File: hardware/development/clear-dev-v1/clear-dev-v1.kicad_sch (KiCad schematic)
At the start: 86 parts, among them J1 USB_B_Micro, J10 Conn_01x28_Pin, J11 Conn_01x28_Pin, J12 Conn_01x02_Pin, J2 Conn_01x02_Pin, J3 Conn_01x02_Pin, J4 Conn_01x03_Pin, J5 Conn_01x02_Pin, J6 Conn_01x02_Pin, J7 Conn_01x06_Pin, J8 Conn_01x02_Pin, J9 Conn_01x02_Pin, SW1 SW_Push - SKQGADE010, T1 Logo, T2 Logo, U1 FT232H, U10 DS1086LU, U2 SN74LVC1G125DCKR, U3 SN74LVC1G125DCKR, U4 SN74LVC1G125DCKR, U5 TAR5SxxU, U6 TAR5SxxU, U7 W25Q32FVSS, U8 M.2-CONNECTOR-E, U9 TMUX4053-BQB, X1 DSC6001_10MHZ, Y1 12MHz

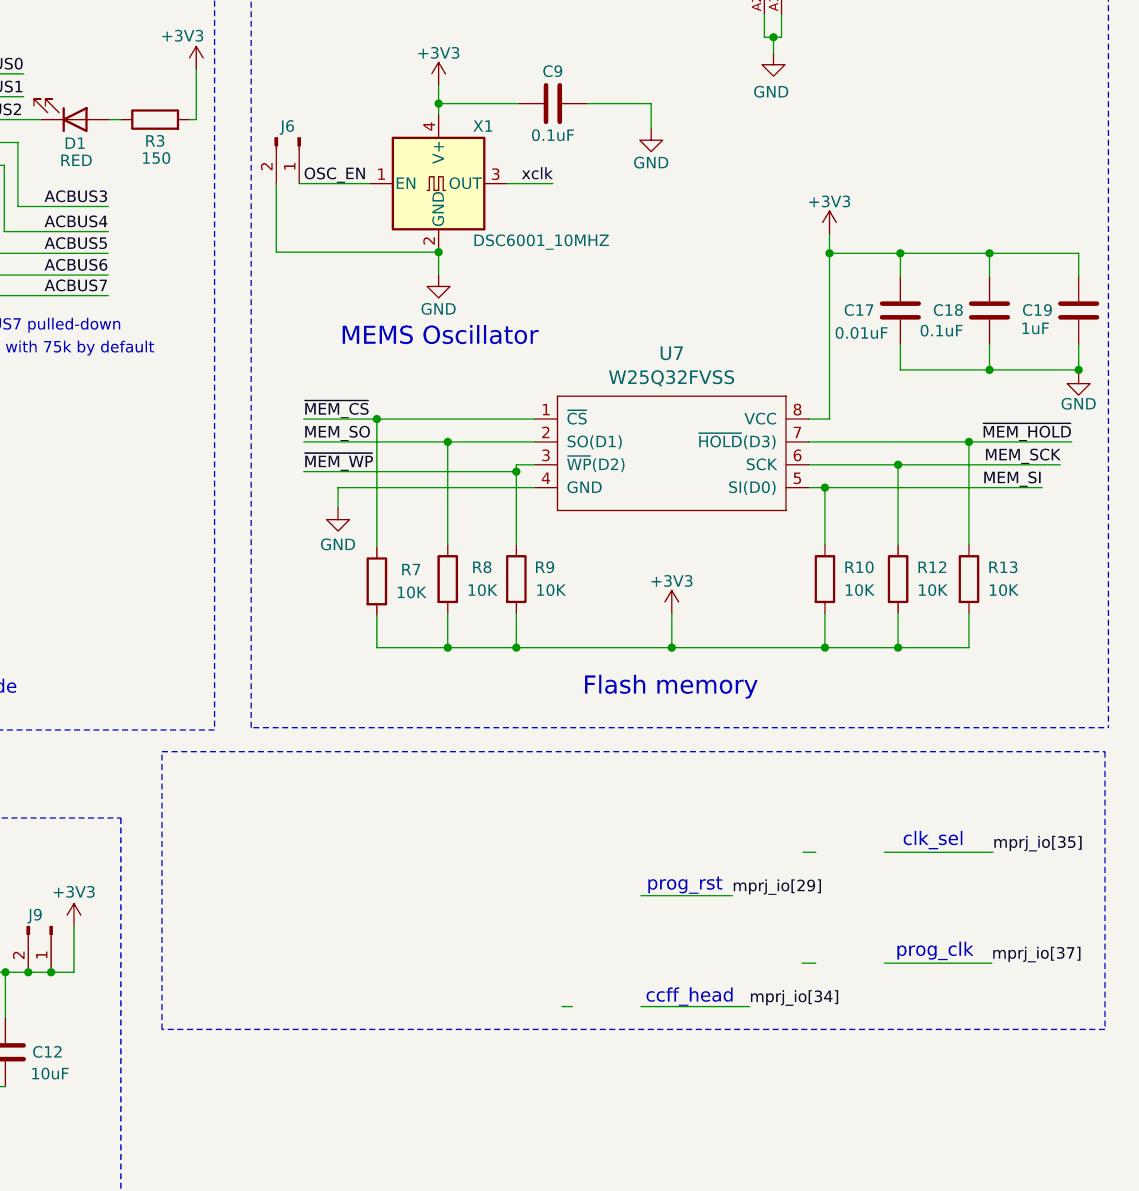
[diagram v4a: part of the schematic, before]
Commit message: update clear dev board to REV 1B after layout review
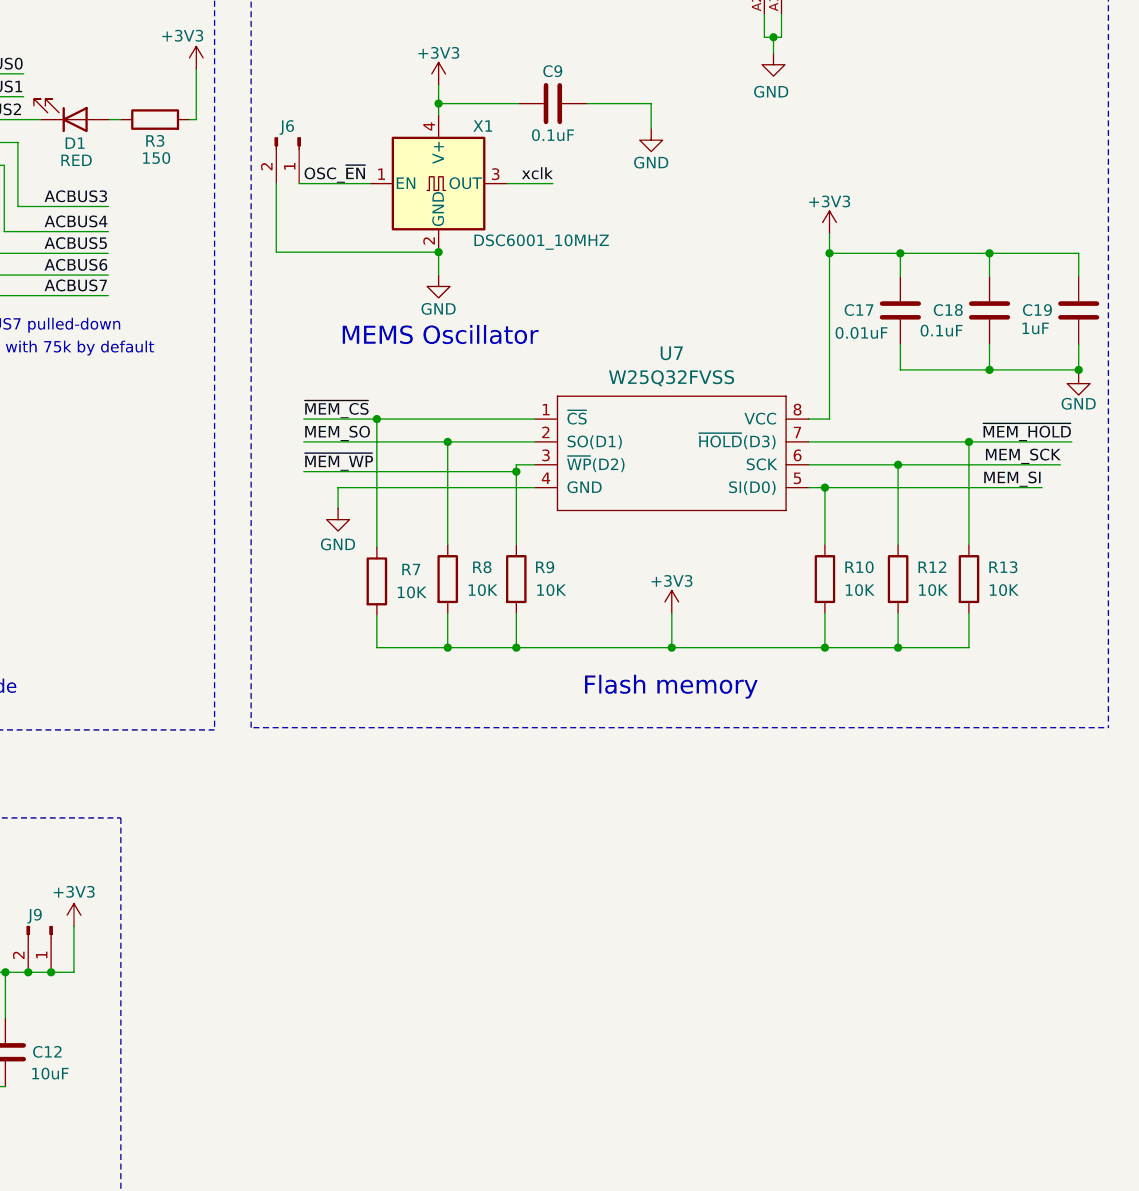
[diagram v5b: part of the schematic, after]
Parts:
- J3, J5, J8, J9: footprint Connector_PinHeader_2.54mm:PinHeader_1x02_P2.54mm_Vertical -> Caravel_Board:Shorted_PinHeader_1x02_P2.54mm_Vertical
- JP1, JP2, JP3, JP4, JP5, JP6: footprint SolderJumper-2_P1.3mm_Bridged_Pad1.0x1.5mm -> Jumper:SolderJumper-2_P1.3mm_Bridged_Pad1.0x1.5mm
- U2, U3, U4: footprint SOT65P210X110-5N -> strive_foot_prints:SOT65P210X110-5N
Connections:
- net OSC_EN renamed OSC_~{EN}
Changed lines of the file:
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@@
     (stroke (width 0) (type default))
   )
-  (wire (pts (xy 353.187 248.158) (xy 365.252 248.158))
-    (stroke (width 0) (type default))
-  )
   (wire (pts (xy 272.161 106.426) (xy 275.971 106.426))
     (stroke (width 0) (type default))
@@
     (stroke (width 0) (type default))
   )
-  (wire (pts (xy 353.187 235.839) (xy 363.347 235.839))
-    (stroke (width 0) (type default))
-  )
   (wire (pts (xy 121.412 41.148) (xy 129.032 41.148))
     (stroke (width 0) (type default))
@@
     (stroke (width 0) (type default))
   )
-  (wire (pts (xy 380.238 243.332) (xy 392.176 243.332))
-    (stroke (width 0) (type default))
-  )
   (wire (pts (xy 401.828 167.005) (xy 401.828 164.465))
     (stroke (width 0) (type default))
@@
     (stroke (width 0) (type default))
   )
-  (wire (pts (xy 380.238 231.013) (xy 392.303 231.013))
-    (stroke (width 0) (type default))
-  )
   (wire (pts (xy 391.922 177.419) (xy 391.922 174.625))
     (stroke (width 0) (type default))
@@
     (stroke (width 0) (type default))
   )
-  (wire (pts (xy 371.221 231.013) (xy 372.618 231.013))
-    (stroke (width 0) (type default))
-  )
   (wire (pts (xy 35.56 46.228) (xy 24.384 46.228))
     (stroke (width 0) (type default))
@@
     (stroke (width 0) (type default))
   )
-  (wire (pts (xy 344.424 248.158) (xy 345.567 248.158))
-    (stroke (width 0) (type default))
-  )
   (wire (pts (xy 54.61 79.248) (xy 60.96 79.248))
     (stroke (width 0) (type default))
@@
     (stroke (width 0) (type default))
   )
-  (wire (pts (xy 371.094 243.332) (xy 372.618 243.332))
-    (stroke (width 0) (type default))
-  )
   (polyline (pts (xy 295.402 227.203) (xy 295.402 279.273))
     (stroke (width 0) (type dash))
@@
     (stroke (width 0) (type default))
   )
-  (rectangle (start 299.974 219.837) (end 404.749 250.698)
-    (stroke (width 0) (type dash))
-    (fill (type none))
-  )
   (text "USB to Serial" (at 191.6176 80.2386 0)
     (effects (font (size 3.5 3.5) (thickness 0.7) bold italic) (justify left bottom))
@@
     (effects (font (size 1.5 1.5)) (justify left bottom))
   )
-  (text "ccff_head" (at 353.695 248.031 0)
-    (effects (font (size 1.5 1.5)) (justify left bottom))
-  )
   (text "Serial Display" (at 81.915 58.293 0)
     (effects (font (size 2 2)) (justify left bottom))
@@
     (effects (font (size 1.5 1.5)) (justify left bottom))
   )
-  (text "prog_clk" (at 381.508 242.951 0)
-    (effects (font (size 1.5 1.5)) (justify left bottom))
-  )
   (text "FTDI and Caravel IOs interfaces with e-FPGA IOs on Caravel"
     (at 92.964 199.39 0)
@@
     (effects (font (size 2 2)) (justify left bottom))
   )
-  (text "prog_rst" (at 353.822 235.585 0)
-    (effects (font (size 1.5 1.5)) (justify left bottom))
-  )
   (text "*ACBUS7 pulled-down" (at 276.5806 173.3296 0)
     (effects (font (size 1.25 1.25)) (justify left bottom))
@@
     (effects (font (size 2 2)) (justify left bottom))
   )
-  (text "clk_sel" (at 382.27 230.632 0)
-    (effects (font (size 1.5 1.5)) (justify left bottom))
-  )
   (text "clk_sel" (at 126.873 190.4746 0)
     (effects (font (size 1.5 1.5)) (justify left bottom))
@@
     (effects (font (size 1.27 1.27)) (justify right bottom))
   )
-  (label "mprj_io[34]" (at 365.252 248.158 0) (fields_autoplaced)
-    (effects (font (size 1.27 1.27)) (justify left bottom))
-  )
   (label "~{MEM_HOLD}" (at 401.066 185.42 180) (fields_autoplaced)
     (effects (font (size 1.27 1.27)) (justify right bottom))
@@
     (effects (font (size 1.27 1.27)) (justify right bottom))
   )
-  (label "mprj_io[35]" (at 392.303 231.013 0) (fields_autoplaced)
-    (effects (font (size 1.27 1.27)) (justify left bottom))
-  )
   (label "USB_SI" (at 71.12 196.723 180) (fields_autoplaced)
     (effects (font (size 1.27 1.27)) (justify right bottom))
@@
     (effects (font (size 1.27 1.27)) (justify right bottom))
   )
-  (label "mprj_io[37]" (at 392.176 243.332 0) (fields_autoplaced)
-    (effects (font (size 1.27 1.27)) (justify left bottom))
-  )
   (label "mprj_io[5]_ser_rx" (at 77.724 48.768 180) (fields_autoplaced)
     (effects (font (size 1.27 1.27)) (justify right bottom))
@@
     (effects (font (size 1 1)) (justify left bottom))
   )
-  (label "mprj_io[29]" (at 363.347 235.839 0) (fields_autoplaced)
-    (effects (font (size 1.27 1.27)) (justify left bottom))
-  )
   (label "USB_CS1" (at 31.115 144.145 0) (fields_autoplaced)
     (effects (font (size 1.27 1.27)) (justify left bottom))
@@
     (effects (font (size 1.27 1.27)) (justify left bottom))
   )
-  (label "OSC_EN" (at 315.722 156.718 0) (fields_autoplaced)
+  (label "OSC_~{EN}" (at 315.722 156.718 0) (fields_autoplaced)
     (effects (font (size 1.27 1.27)) (justify left bottom))
   )
@@
       (effects (font (size 1.27 1.27)) hide)
     )
-    (property "Footprint" "SolderJumper-2_P1.3mm_Bridged_Pad1.0x1.5mm" (at 160.274 181.229 0)
+    (property "Footprint" "Jumper:SolderJumper-2_P1.3mm_Bridged_Pad1.0x1.5mm" (at 160.274 181.229 0)
       (effects (font (size 1.27 1.27)) hide)
     )
@@
       (effects (font (size 1.27 1.27)) hide)
     )
-    (property "Footprint" "SolderJumper-2_P1.3mm_Bridged_Pad1.0x1.5mm" (at 160.274 178.308 0)
+    (property "Footprint" "Jumper:SolderJumper-2_P1.3mm_Bridged_Pad1.0x1.5mm" (at 160.274 178.308 0)
       (effects (font (size 1.27 1.27)) hide)
     )
@@
       (effects (font (size 1.27 1.27)) hide)
     )
-    (property "Footprint" "SolderJumper-2_P1.3mm_Bridged_Pad1.0x1.5mm" (at 160.274 184.277 0)
+    (property "Footprint" "Jumper:SolderJumper-2_P1.3mm_Bridged_Pad1.0x1.5mm" (at 160.274 184.277 0)
       (effects (font (size 1.27 1.27)) hide)
     )
@@
       (effects (font (size 1.27 1.27)))
     )
-    (property "Footprint" "SOT65P210X110-5N" (at 140.97 148.844 0)
+    (property "Footprint" "strive_foot_prints:SOT65P210X110-5N" (at 140.97 148.844 0)
       (effects (font (size 1.27 1.27)) (justify left bottom) hide)
     )
@@
       (effects (font (size 1.27 1.27)) hide)
     )
-    (property "Footprint" "Connector_PinHeader_2.54mm:PinHeader_1x02_P2.54mm_Vertical" (at 124.46 75.438 0)
+    (property "Footprint" "Caravel_Board:Shorted_PinHeader_1x02_P2.54mm_Vertical" (at 124.46 75.438 0)
       (effects (font (size 1.27 1.27)) hide)
     )
@@
       (effects (font (size 1.27 1.27)) hide)
     )
-    (property "Footprint" "SolderJumper-2_P1.3mm_Bridged_Pad1.0x1.5mm" (at 160.274 190.627 0)
+    (property "Footprint" "Jumper:SolderJumper-2_P1.3mm_Bridged_Pad1.0x1.5mm" (at 160.274 190.627 0)
       (effects (font (size 1.27 1.27)) hide)
     )
@@
       (effects (font (size 1.27 1.27)) hide)
     )
-    (property "Footprint" "Connector_PinHeader_2.54mm:PinHeader_1x02_P2.54mm_Vertical" (at 226.314 239.776 0)
+    (property "Footprint" "Caravel_Board:Shorted_PinHeader_1x02_P2.54mm_Vertical" (at 226.314 239.776 0)
       (effects (font (size 1.27 1.27)) hide)
     )
@@
       (effects (font (size 1.27 1.27)))
     )
-    (property "Footprint" "SOT65P210X110-5N" (at 161.29 130.81 0)
+    (property "Footprint" "strive_foot_prints:SOT65P210X110-5N" (at 161.29 130.81 0)
       (effects (font (size 1.27 1.27)) (justify left bottom) hide)
     )
@@
       (effects (font (size 1.27 1.27)))
     )
-    (property "Footprint" "SOT65P210X110-5N" (at 54.737 196.723 0)
+    (property "Footprint" "strive_foot_prints:SOT65P210X110-5N" (at 54.737 196.723 0)
       (effects (font (size 1.27 1.27)) (justify left bottom) hide)
     )
@@
       (effects (font (size 1.27 1.27)) hide)
     )
-    (property "Footprint" "SolderJumper-2_P1.3mm_Bridged_Pad1.0x1.5mm" (at 160.274 193.929 0)
+    (property "Footprint" "Jumper:SolderJumper-2_P1.3mm_Bridged_Pad1.0x1.5mm" (at 160.274 193.929 0)
       (effects (font (size 1.27 1.27)) hide)
     )
@@
       (effects (font (size 1.27 1.27)) hide)
     )
-    (property "Footprint" "Connector_PinHeader_2.54mm:PinHeader_1x02_P2.54mm_Vertical" (at 146.05 75.438 0)
+    (property "Footprint" "Caravel_Board:Shorted_PinHeader_1x02_P2.54mm_Vertical" (at 146.05 75.438 0)
       (effects (font (size 1.27 1.27)) hide)
     )
@@
       (effects (font (size 1.27 1.27)) hide)
     )
-    (property "Footprint" "Connector_PinHeader_2.54mm:PinHeader_1x02_P2.54mm_Vertical" (at 287.655 239.268 0)
+    (property "Footprint" "Caravel_Board:Shorted_PinHeader_1x02_P2.54mm_Vertical" (at 287.655 239.268 0)
       (effects (font (size 1.27 1.27)) hide)
     )
@@
       (effects (font (size 1.27 1.27)) hide)
     )
-    (property "Footprint" "SolderJumper-2_P1.3mm_Bridged_Pad1.0x1.5mm" (at 160.274 187.452 0)
+    (property "Footprint" "Jumper:SolderJumper-2_P1.3mm_Bridged_Pad1.0x1.5mm" (at 160.274 187.452 0)
       (effects (font (size 1.27 1.27)) hide)
     )
